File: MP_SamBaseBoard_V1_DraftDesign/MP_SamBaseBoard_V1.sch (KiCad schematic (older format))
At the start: 116 parts, among them J1 MOTOR-A_CONN, J10 P1_CONN, J11 I2C_CONN, J12 I2C_CONN, J13 SAM_SWD, J14 WS2812_EXT, J15 PWR_JACK, J2 MOTOR-B_CONN, J3 Adafruit_Feather_CONN, J4 uSD_Card, J5 Conn_01x02, J6 Conn_01x02, J7 SERVO_CONN, J8 P3_CONN, J9 P2_CONN, Q1 DMP3098L, SW1 RESET, SW2 3v3_PWR_SW, SW3 SW1, SW4 SW2, U1 ESP32-WROOM-32, U10 MPU-6050, U11 IRFHM9331PbF, U12 BD5291FVE-GTR, U2 ATSAMD51J19A-A, U3 74LVC1G125, U4 TPS62135, U5 TPS62086, U6 MAX98357AETE, U7 DRV8833RTY, U8 HDC1080, U9 MCP73871-1CC, Y1 Crystal

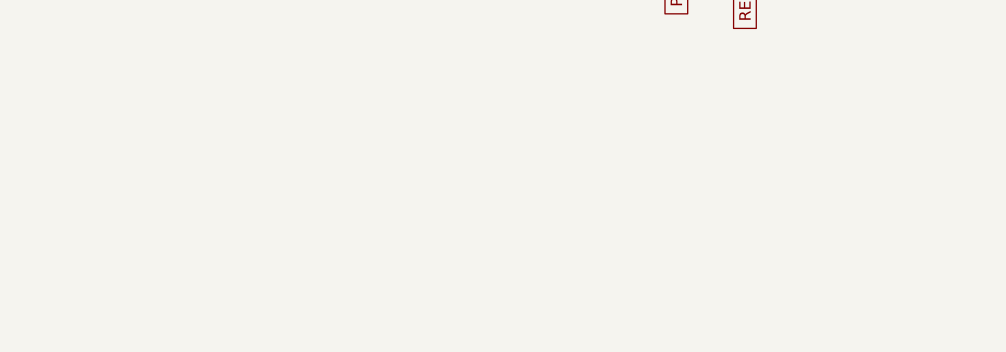
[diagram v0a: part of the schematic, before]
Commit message: update schematic
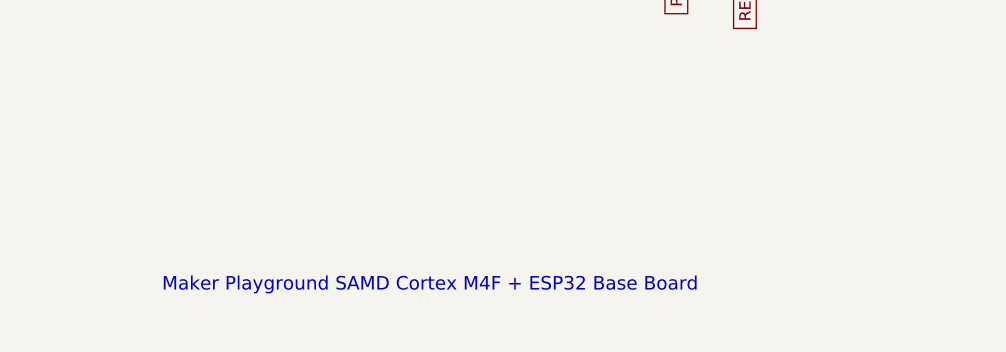
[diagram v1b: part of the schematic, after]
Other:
- note added: "Maker Playground SAMD Cortex M4F + ESP32 Base Board"
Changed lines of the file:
@@
 Wire Wire Line
 	5500 5800 5500 5900
+Text Notes 12200 10950 0    59   ~ 0
+Maker Playground SAMD Cortex M4F + ESP32 Base Board
 $EndSCHEMATC

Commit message: Finalize schematic
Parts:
- D6, D7: footprint LED_SMD:LED_WS2812B_PLCC4_5.0x5.0mm_P3.2mm -> GiraffeTech-LED:WS2812B_MINI
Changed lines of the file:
@@
 F 0 "D6" H 10600 6350 50  0000 L CNN
 F 1 "WS2812B" H 10850 6350 50  0000 L CNN
-F 2 "LED_SMD:LED_WS2812B_PLCC4_5.0x5.0mm_P3.2mm" H 10850 5800 50  0001 L TNN
+F 2 "GiraffeTech-LED:WS2812B_MINI" H 10850 5800 50  0001 L TNN
 F 3 "https://cdn-shop.adafruit.com/datasheets/WS2812B.pdf" H 10900 5725 50  0001 L TNN
 	1    10800 6100
@@
 F 0 "D7" H 11300 6350 50  0000 L CNN
 F 1 "WS2812B" H 11550 6350 50  0000 L CNN
-F 2 "LED_SMD:LED_WS2812B_PLCC4_5.0x5.0mm_P3.2mm" H 11550 5800 50  0001 L TNN
+F 2 "GiraffeTech-LED:WS2812B_MINI" H 11550 5800 50  0001 L TNN
 F 3 "https://cdn-shop.adafruit.com/datasheets/WS2812B.pdf" H 11600 5725 50  0001 L TNN
 	1    11500 6100

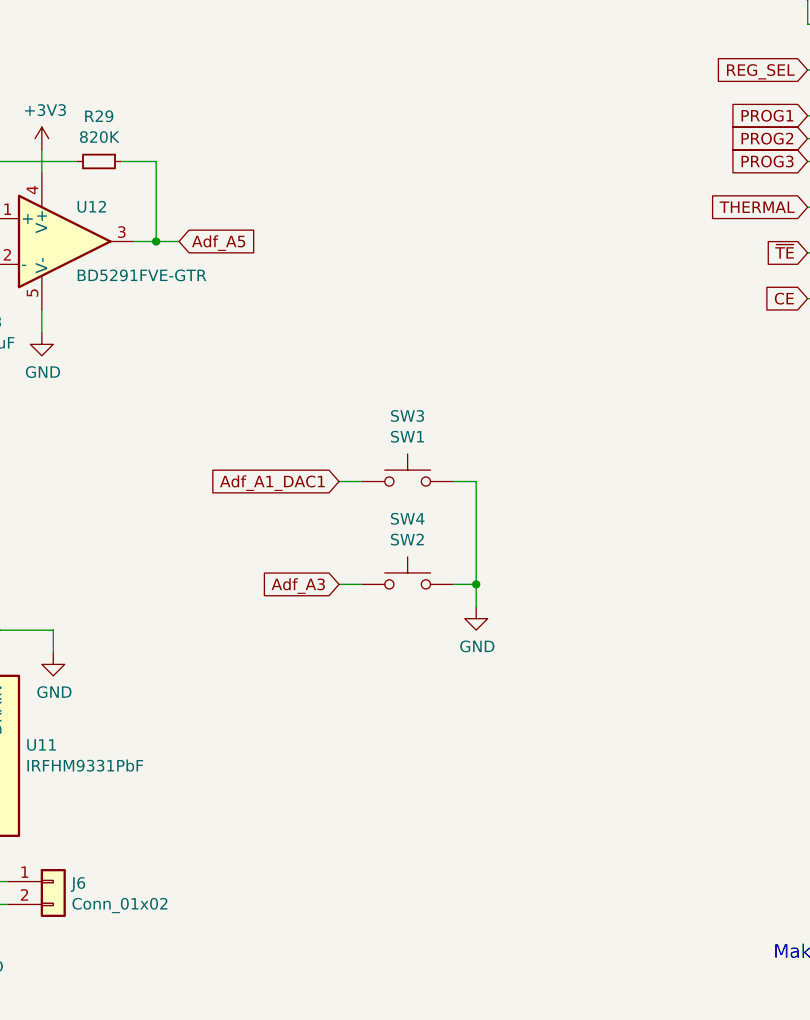
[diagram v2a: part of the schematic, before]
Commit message: Schematic done, update pcb
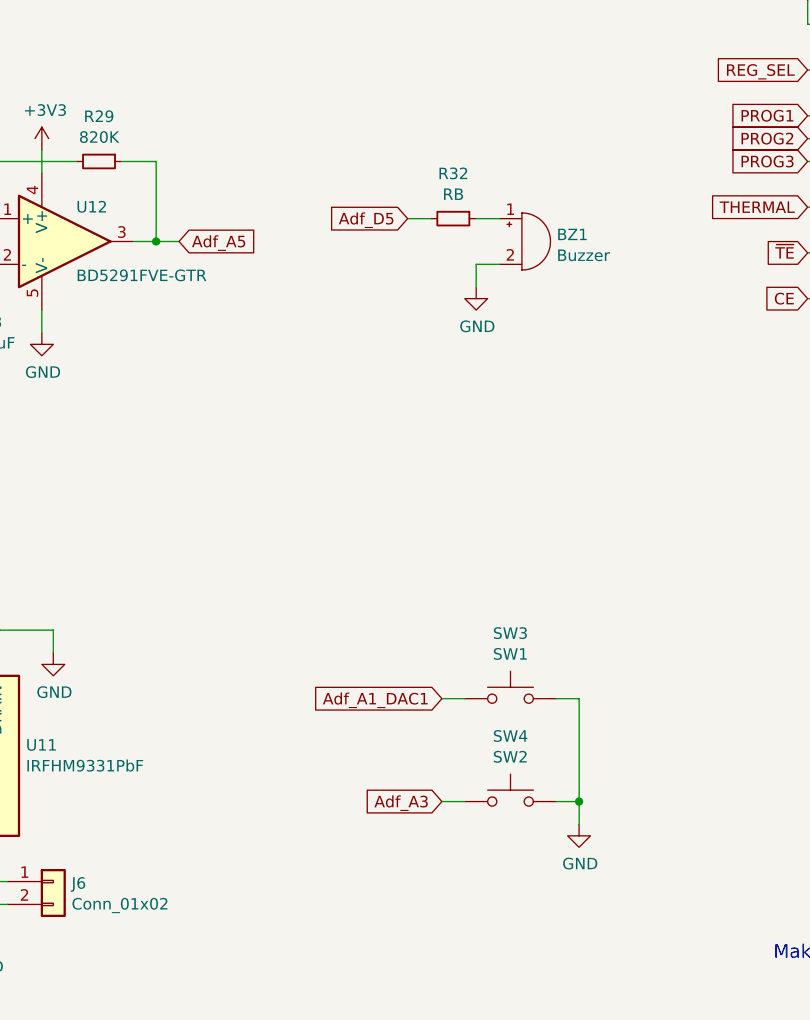
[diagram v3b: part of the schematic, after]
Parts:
- added BZ1: Buzzer, Buzzer_Beeper:MagneticBuzzer_Kobitone_254-EMB84Q-RO, symbol Device:Buzzer
- added R32: RB, Resistor_SMD:R_0603_1608Metric, symbol Device:R_Small
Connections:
- net Adf_D5: now also R32.2
- net GND: now also BZ1.2 (+)
- new net: BZ1.1 (-), R32.1
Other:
- moved on the sheet: SW3, SW4
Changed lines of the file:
@@
 L Switch:SW_Push SW3
 U 1 1 5F59416F
-P 10600 8850
-F 0 "SW3" H 10600 9135 50  0000 C CNN
-F 1 "SW1" H 10600 9044 50  0000 C CNN
-F 2 "Button_Switch_SMD:SW_SPST_B3S-1000" H 10600 9050 50  0001 C CNN
-F 3 "~" H 10600 9050 50  0001 C CNN
-	1    10600 8850
+P 11050 9800
+F 0 "SW3" H 11050 10085 50  0000 C CNN
+F 1 "SW1" H 11050 9994 50  0000 C CNN
+F 2 "Button_Switch_SMD:SW_SPST_B3S-1000" H 11050 10000 50  0001 C CNN
+F 3 "~" H 11050 10000 50  0001 C CNN
+	1    11050 9800
 	1    0    0    -1
 $EndComp
@@
 L Switch:SW_Push SW4
 U 1 1 5F595E63
-P 10600 9300
-F 0 "SW4" H 10600 9585 50  0000 C CNN
-F 1 "SW2" H 10600 9494 50  0000 C CNN
-F 2 "Button_Switch_SMD:SW_SPST_B3S-1000" H 10600 9500 50  0001 C CNN
-F 3 "~" H 10600 9500 50  0001 C CNN
-	1    10600 9300
+P 11050 10250
+F 0 "SW4" H 11050 10535 50  0000 C CNN
+F 1 "SW2" H 11050 10444 50  0000 C CNN
+F 2 "Button_Switch_SMD:SW_SPST_B3S-1000" H 11050 10450 50  0001 C CNN
+F 3 "~" H 11050 10450 50  0001 C CNN
+	1    11050 10250
 	1    0    0    -1
 $EndComp
@@
 L power:GND #PWR0225
 U 1 1 5F5969E8
-P 10900 9400
-F 0 "#PWR0225" H 10900 9150 50  0001 C CNN
-F 1 "GND" H 10905 9227 50  0000 C CNN
-F 2 "" H 10900 9400 50  0001 C CNN
-F 3 "" H 10900 9400 50  0001 C CNN
-	1    10900 9400
-	1    0    0    -1
-$EndComp
-Wire Wire Line
-	10800 8850 10900 8850
-Wire Wire Line
-	10900 8850 10900 9300
-Wire Wire Line
-	10800 9300 10900 9300
-Connection ~ 10900 9300
-Wire Wire Line
-	10900 9300 10900 9400
-Text GLabel 10300 9300 0    50   Input ~ 0
+P 11350 10350
+F 0 "#PWR0225" H 11350 10100 50  0001 C CNN
+F 1 "GND" H 11355 10177 50  0000 C CNN
+F 2 "" H 11350 10350 50  0001 C CNN
+F 3 "" H 11350 10350 50  0001 C CNN
+	1    11350 10350
+	1    0    0    -1
+$EndComp
+Wire Wire Line
+	11250 9800 11350 9800
+Wire Wire Line
+	11350 9800 11350 10250
+Wire Wire Line
+	11250 10250 11350 10250
+Connection ~ 11350 10250
+Wire Wire Line
+	11350 10250 11350 10350
+Text GLabel 10750 10250 0    50   Input ~ 0
 Adf_A3
-Text GLabel 10300 8850 0    50   Input ~ 0
+Text GLabel 10750 9800 0    50   Input ~ 0
 Adf_A1_DAC1
 Wire Wire Line
-	10300 9300 10400 9300
-Wire Wire Line
-	10300 8850 10400 8850
+	10750 10250 10850 10250
+Wire Wire Line
+	10750 9800 10850 9800
 $Comp
 L LED:WS2812B D6
@@
 Text Notes 12200 10950 0    59   ~ 0
 Maker Playground SAMD Cortex M4F + ESP32 Base Board
+Text GLabel 10600 7700 0    50   Input ~ 0
+Adf_D5
+$Comp
+L Device:Buzzer BZ1
+U 1 1 5ED7BCD8
+P 11100 7800
+F 0 "BZ1" H 11252 7829 50  0000 L CNN
+F 1 "Buzzer" H 11252 7738 50  0000 L CNN
+F 2 "Buzzer_Beeper:MagneticBuzzer_Kobitone_254-EMB84Q-RO" V 11075 7900 50  0001 C CNN
+F 3 "~" V 11075 7900 50  0001 C CNN
+	1    11100 7800
+	1    0    0    -1
+$EndComp
+$Comp
+L Device:R_Small R32
+U 1 1 5ED7E16B
+P 10800 7700
+F 0 "R32" V 10604 7700 50  0000 C CNN
+F 1 "RB" V 10695 7700 50  0000 C CNN
+F 2 "Resistor_SMD:R_0603_1608Metric" H 10800 7700 50  0001 C CNN
+F 3 "~" H 10800 7700 50  0001 C CNN
+	1    10800 7700
+	0    1    1    0
+$EndComp
+Wire Wire Line
+	10600 7700 10700 7700
+Wire Wire Line
+	10900 7700 11000 7700
+$Comp
+L power:GND #PWR0232
+U 1 1 5EE434AE
+P 10900 8000
+F 0 "#PWR0232" H 10900 7750 50  0001 C CNN
+F 1 "GND" H 10905 7827 50  0000 C CNN
+F 2 "" H 10900 8000 50  0001 C CNN
+F 3 "" H 10900 8000 50  0001 C CNN
+	1    10900 8000
+	1    0    0    -1
+$EndComp
+Wire Wire Line
+	10900 8000 10900 7900
+Wire Wire Line
+	10900 7900 11000 7900
 $EndSCHEMATC

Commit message: update
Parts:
- added D8: PWR_LED, LED_SMD:LED_0603_1608Metric, symbol Device:LED
- added J16: USB_B_Micro, GiraffeTech-Connector:USB_Micro-B_Amphenol_10118193_Horizontal, symbol Connector:USB_B_Micro
- added J17: BATT_CONN, GiraffeTech-Connector:TerminalBlock_Dinkle_ED350V_1x02_P3.50mm_Horizontal, symbol Connector_Generic:Conn_01x02
- added R33, R34: R_USB, Resistor_SMD:R_0603_1608Metric, symbol Device:R_Small
- added R35: 330, Resistor_SMD:R_0603_1608Metric, symbol Device:R_Small
- J5: footprint GiraffeTech-Connector:DINKLE_EK500V-2P -> GiraffeTech-Connector:TerminalBlock_Dinkle_ED350V_1x02_P3.50mm_Horizontal
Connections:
- net +3V3: now also D8.2 (A)
- net +BATT: now also J17.2 (Pin_2)
- net GND: now also D8.1 (K), J16.5 (GND), J16.6 (Shield), J17.1 (Pin_1)
- net USB_DM: now also R34.1
- net USB_DP: now also R33.1
- net USB_PWR_SEL: now also R35.1; no longer R5.1, U3.1, U3.2
- net VBUS: now also J16.1 (VBUS)
- new net: J16.2 (D-), R34.2
- new net: J16.3 (D+), R33.2
- new net USB_ID: J16.4 (ID), R35.2, R5.1, U3.1, U3.2
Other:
- note added: "MOTOR DRIVER"
- note added: "PIEZO BUZZER"
- moved on the sheet: BZ1, C14, C17, C19, C22, C32, C33, L2, MK1, R11, R2, R26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

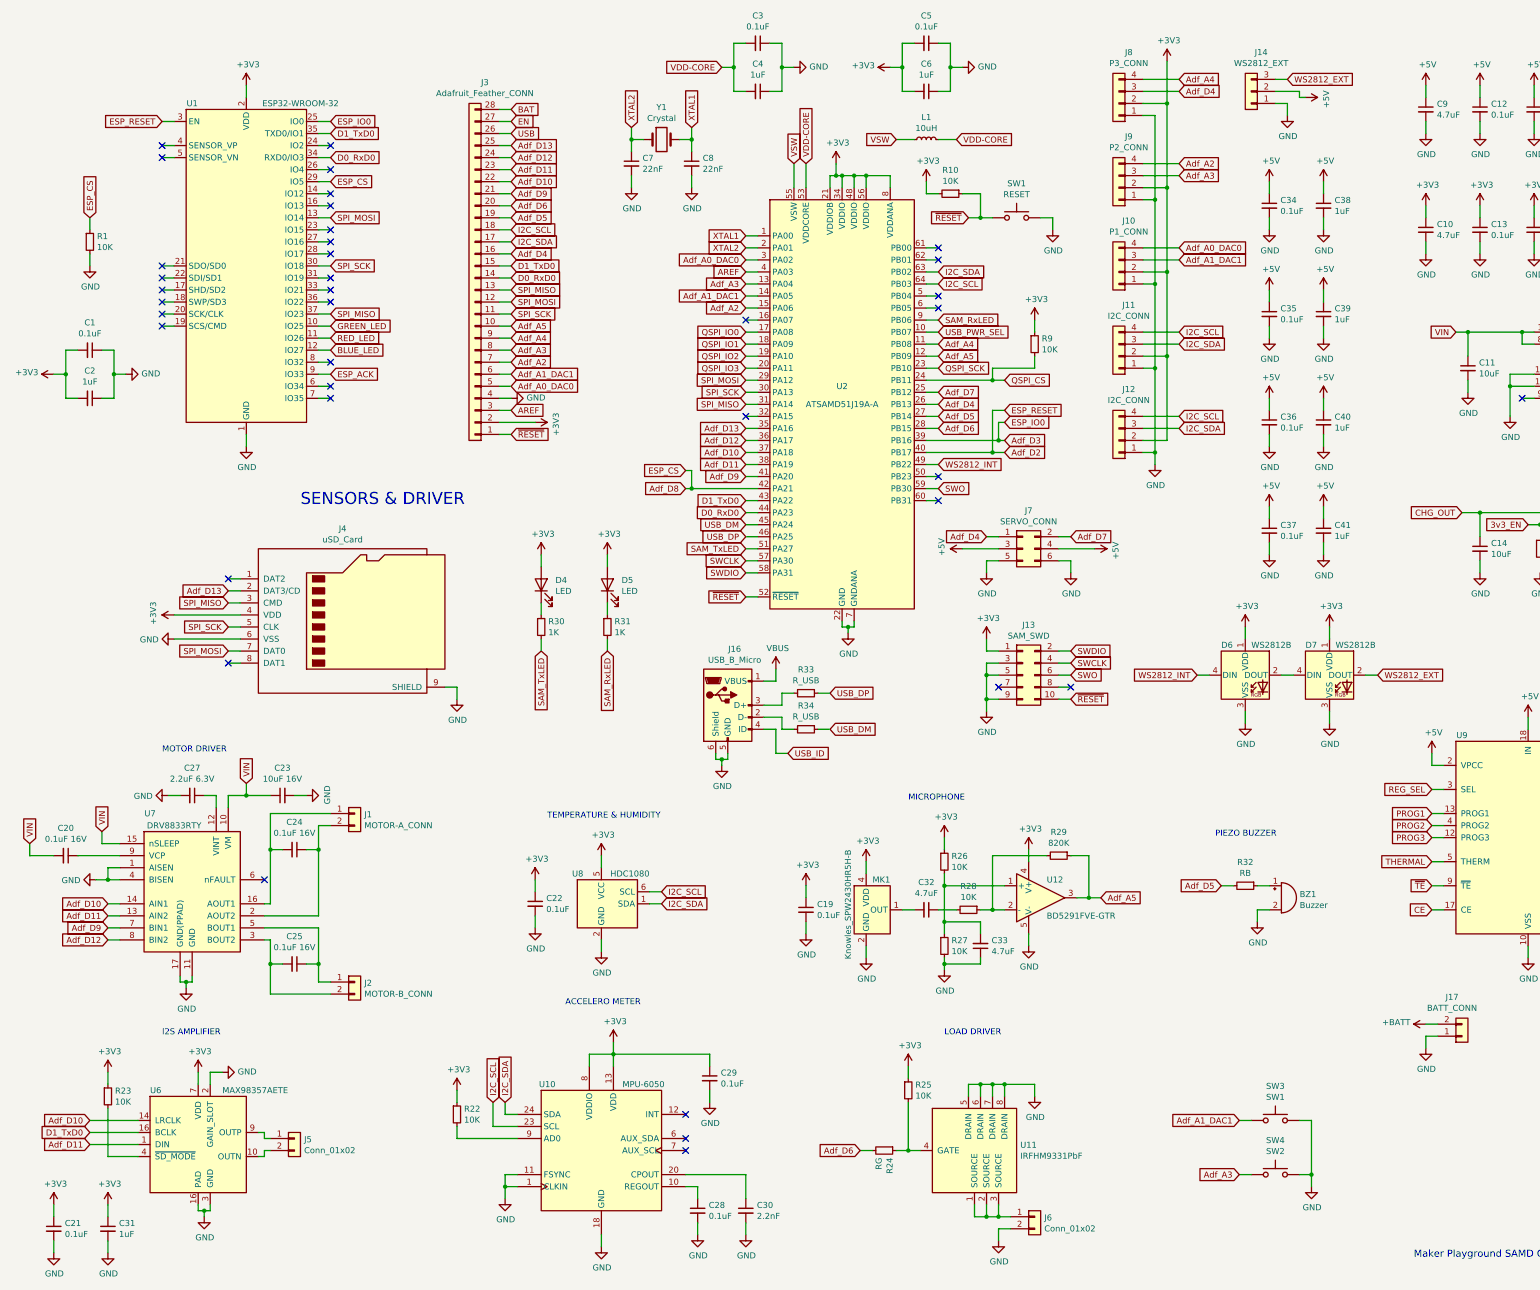
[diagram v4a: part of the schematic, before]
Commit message: Progress in PCB, QSPI flash not complete in schematics
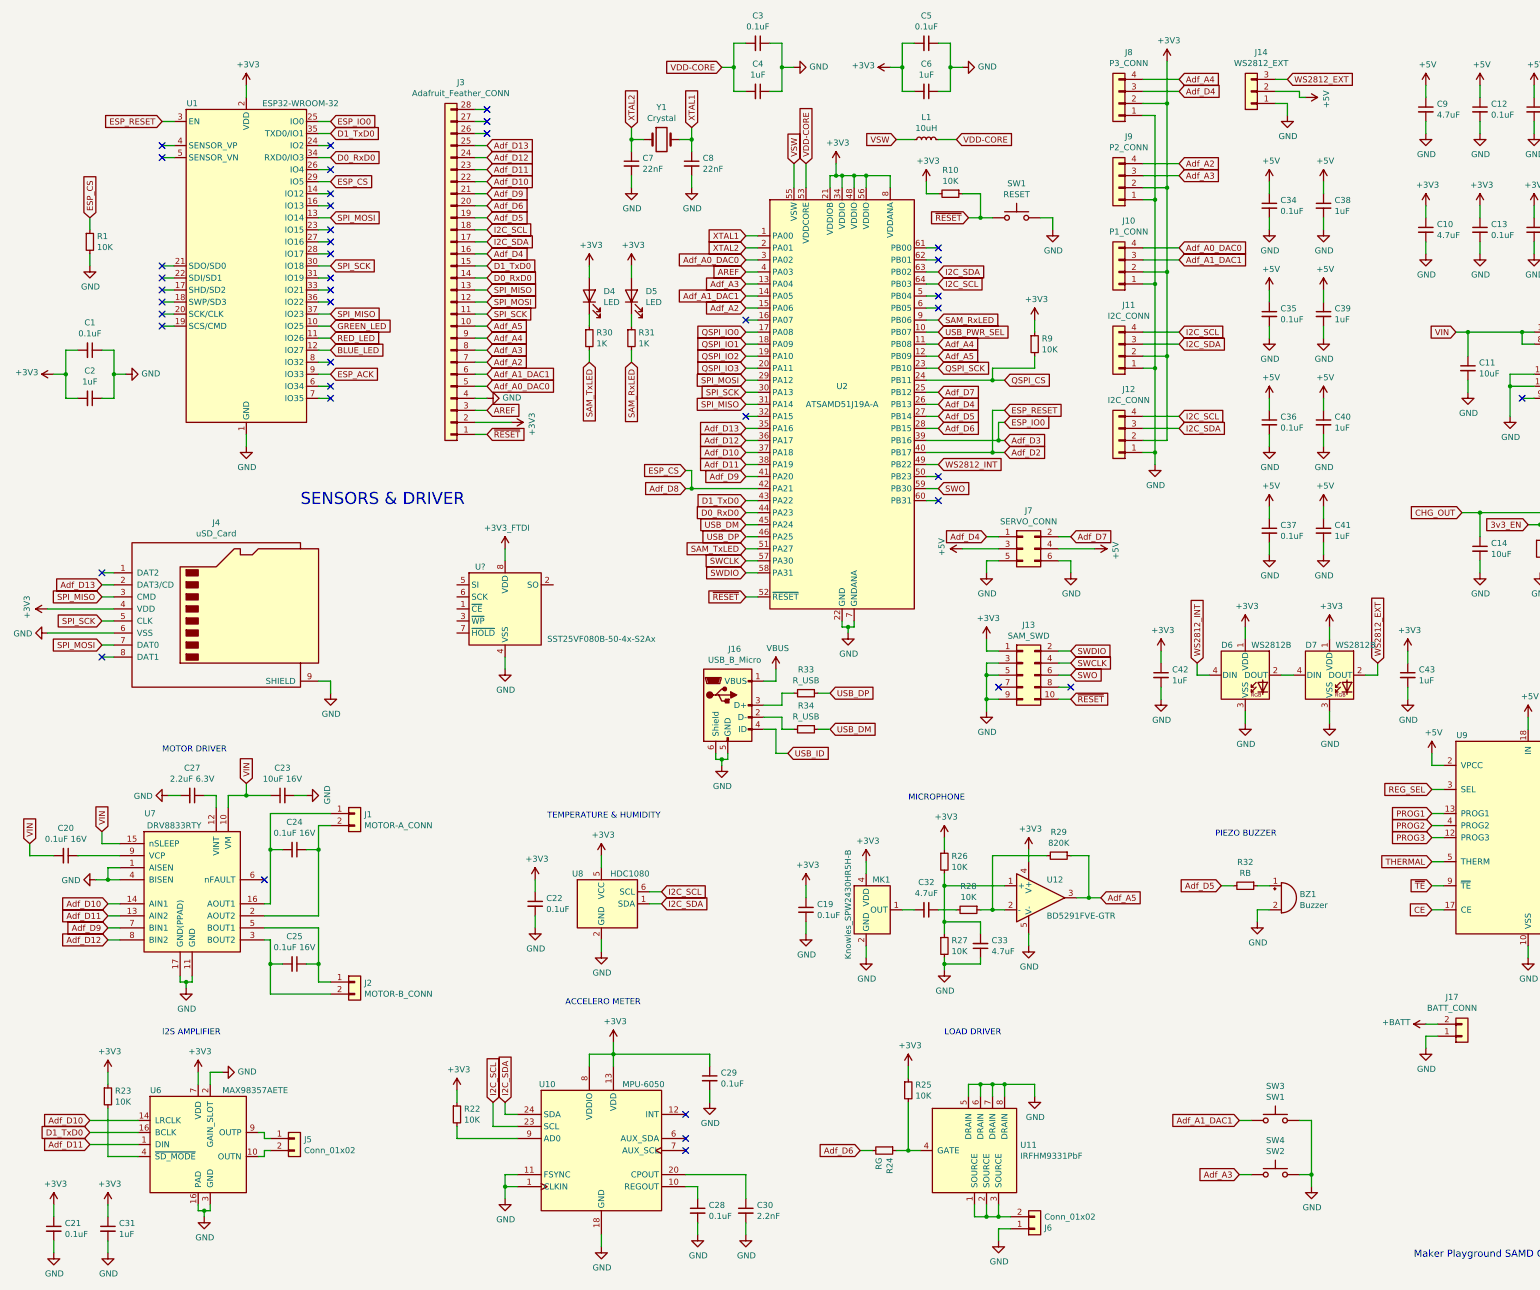
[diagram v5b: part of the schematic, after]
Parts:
- added C42, C43: 1uF, Capacitor_SMD:C_0603_1608Metric, symbol Device:C_Small
- added U?: SST25VF080B-50-4x-S2Ax, Package_SO:SOIC-8_5.275x5.275mm_P1.27mm, symbol Memory_Flash:SST25VF080B-50-4x-S2Ax
- J3: footprint GiraffeTech-Connector:Adafruit-Feather_WoMountPoint -> GiraffeTech-Connector:Adafruit-Feather_WoMountPoint_TypeA
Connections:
- net +3V3: now also C42.1, C43.1
- net GND: now also J6.1 (Pin_1), C42.2, C43.2, U?.4 (VSS); no longer J6.2 (Pin_2)
- net at U11.1 (SOURCE), U11.2 (SOURCE), U11.3 (SOURCE): now also J6.2 (Pin_2); no longer J6.1 (Pin_1)
- net BAT: no longer names the net of J3.28 (Pin_28)
- net EN: no longer names the net of J3.27 (Pin_27)
- net USB: no longer names the net of J3.26 (Pin_26)
- new net +3V3_FTDI: U?.8 (VDD)
- no-connect marks 39 -> 42
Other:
- moved on the sheet: D4, D5, J3, J4, R30, R31
